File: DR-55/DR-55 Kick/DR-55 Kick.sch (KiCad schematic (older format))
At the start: 19 parts

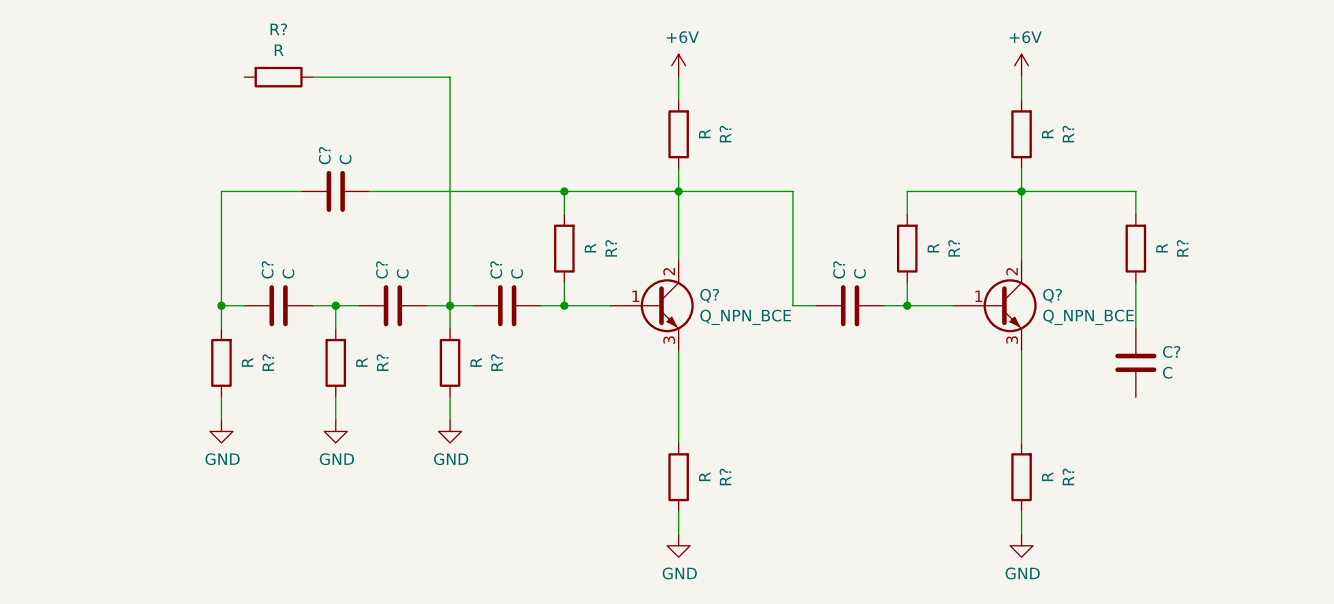
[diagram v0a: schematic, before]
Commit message: Kick update
Updated Kick schematic with two global flags
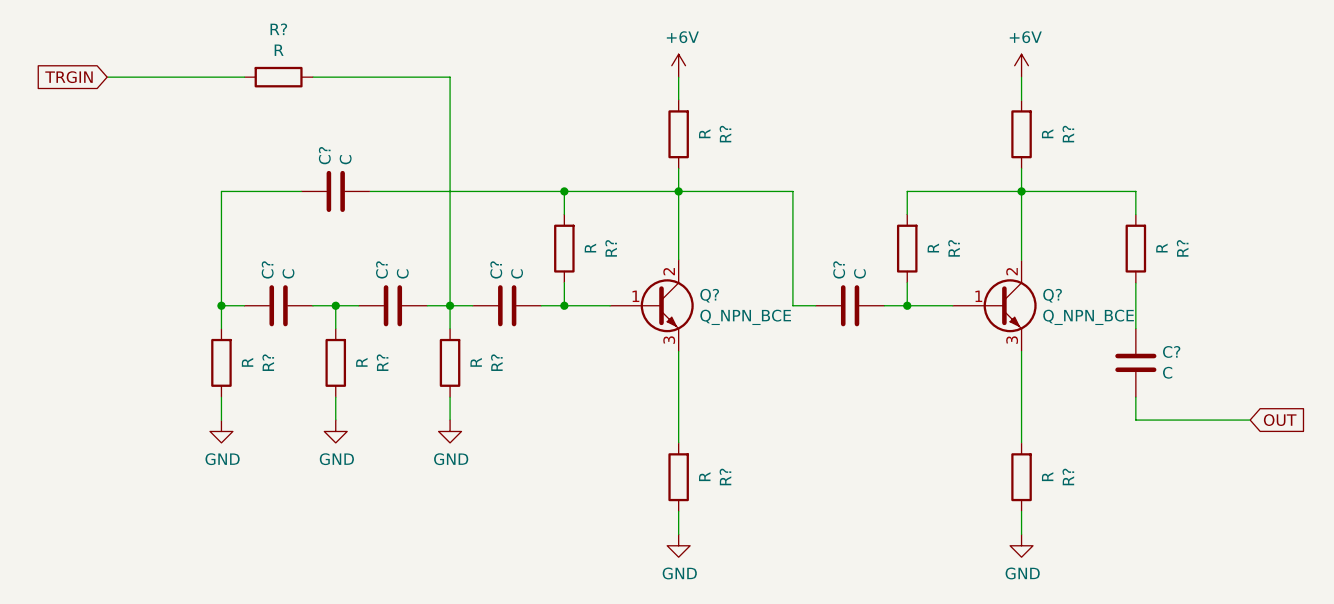
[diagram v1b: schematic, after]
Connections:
- net TRGIN: now reaches R?.2
- net OUT: now reaches C?.2
